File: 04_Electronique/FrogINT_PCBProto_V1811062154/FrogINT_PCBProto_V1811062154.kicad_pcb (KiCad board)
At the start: 2 copper layers, 31 parts, among them J1 USB_B_Mini, J2 Conn_01x01_Female, J3 AVR-JTAG-10, Q1 PMV48XP, Q2 PMV48XP, SW1 SW_SPST, SW2 SW_SPST, U1 NCP1117-5.0_SOT223, U2 LP2985-3.3, U3 ATmega16U4RC-AU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

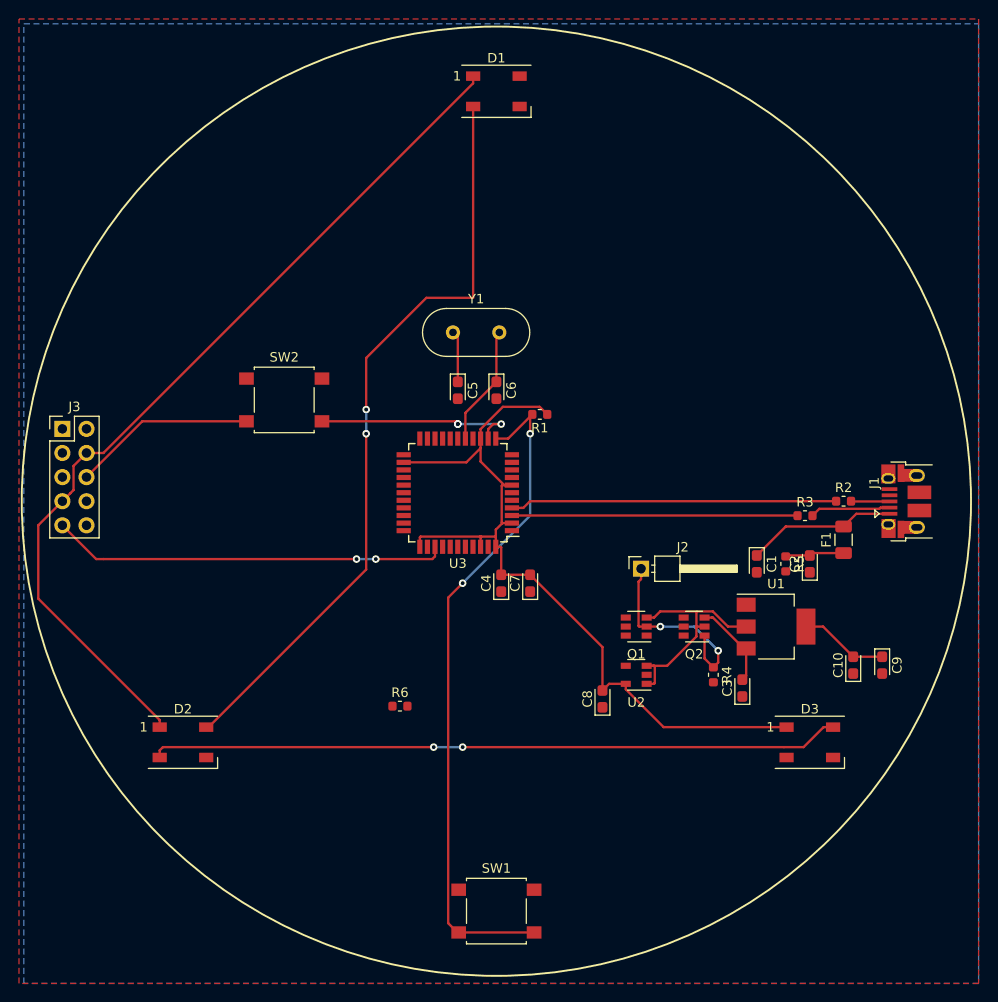
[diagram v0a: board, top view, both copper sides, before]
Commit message: Finalisation du routage + création d'un nouveau routage "Push" pour tester une nouvelle implémentation + Ajout d'un Logo en silkscreen & Copper.
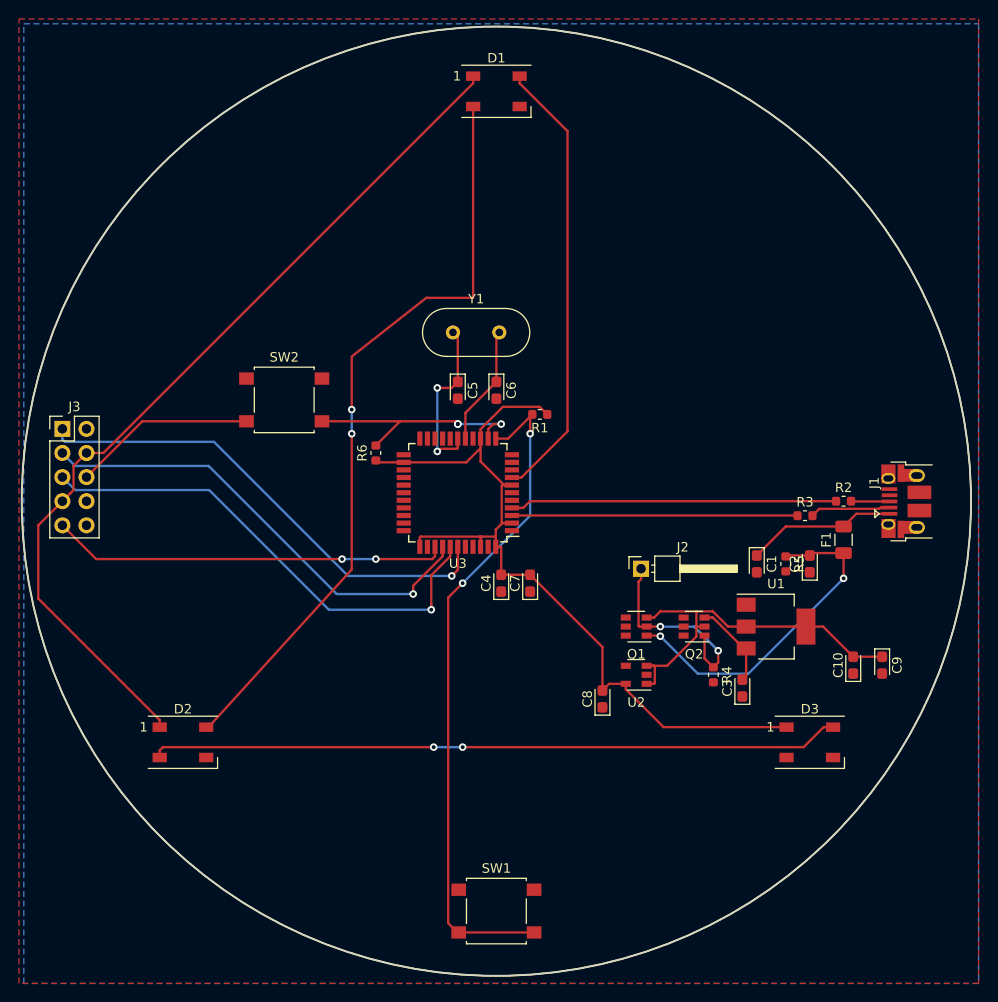
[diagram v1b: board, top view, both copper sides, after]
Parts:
- moved R6 26.8 mm to (133.9, 93.2), turned to 90 degrees
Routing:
- net Net-(J3-Pad5): track 0.00 -> 52.1 mm, vias 0 -> 1
- net Net-(J3-Pad1): track 0.00 -> 51.4 mm, vias 0 -> 1
- net Net-(J3-Pad3): track 0.00 -> 49.4 mm, vias 0 -> 1
- net Net-(D1-Pad4): track 0.00 -> 47.4 mm
- net VBUS: track 6.24 -> 35.5 mm, vias 0 -> 2
- net Net-(C5-Pad1): track 5.42 -> 17.8 mm, vias 0 -> 2
- net +5V: track 34.3 -> 40.6 mm
- net /reset: track 40.9 -> 44.5 mm
- net +3V3: track 181.5 -> 184.5 mm
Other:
- board outline added: 100 x 100 mm

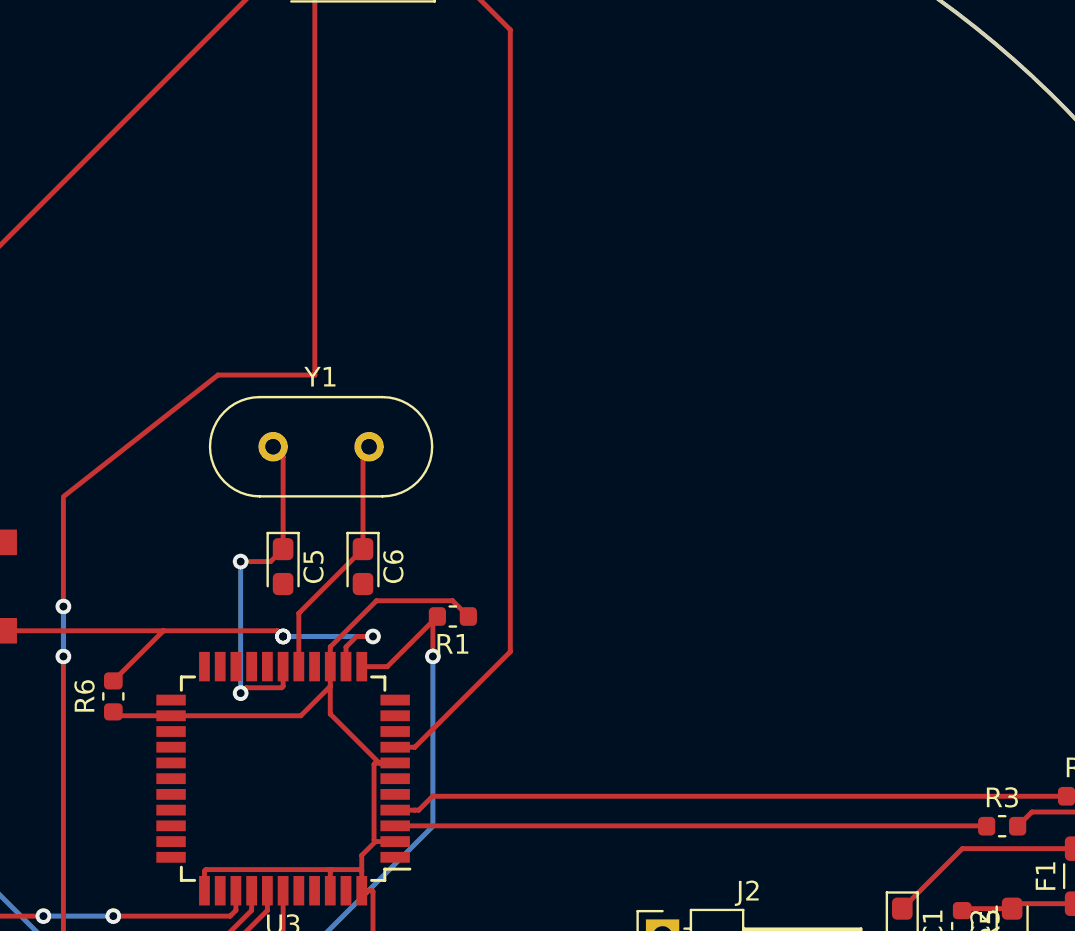
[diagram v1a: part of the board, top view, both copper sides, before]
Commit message: Creation d'un touch Pad et Ajout du composant TTP223.
Création des librairies équivalentes pour le pad dans Samsac.
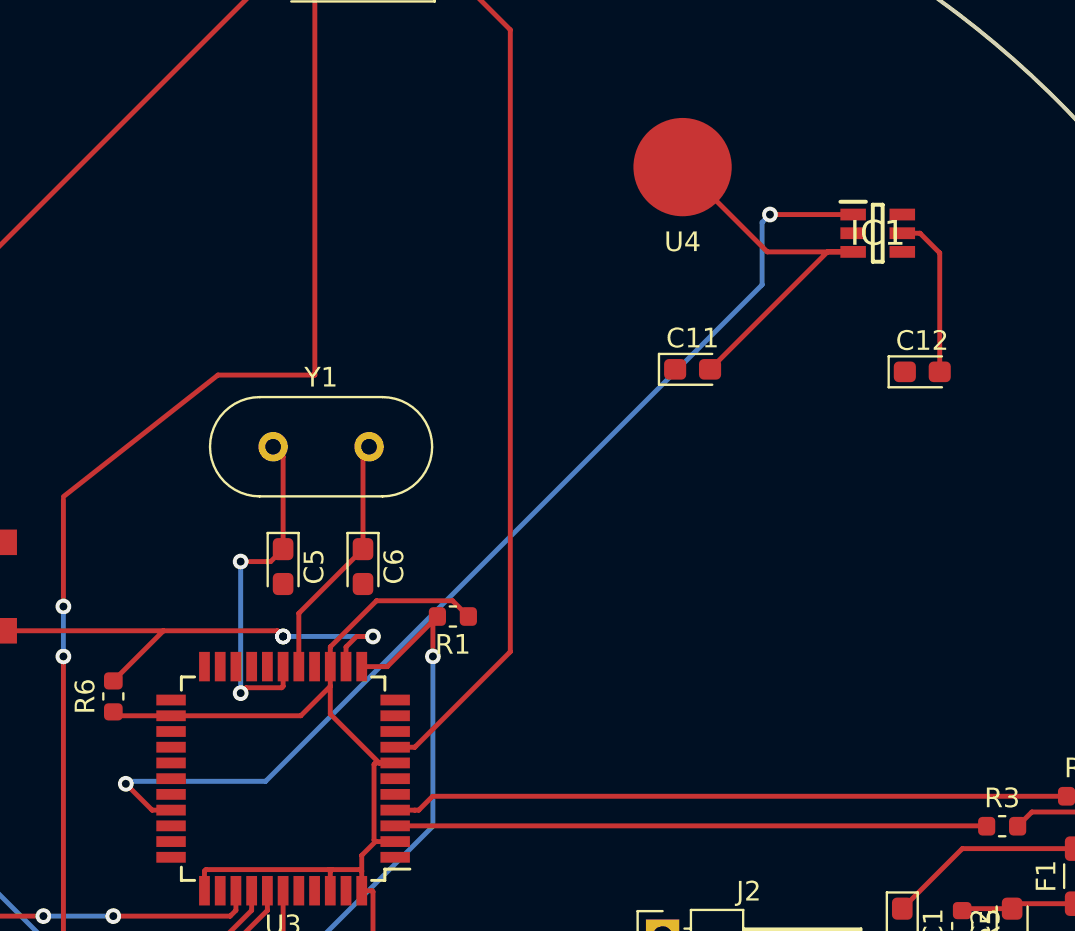
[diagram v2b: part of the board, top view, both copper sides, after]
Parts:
- added C11: 22pF, FTA_FrogINT_Library_Footprint_Package:CP_EIA-2012-12_Kemet-R, F.Cu at (163.3, 76.6)
- added C12: 100nF, FTA_FrogINT_Library_Footprint_Package:CP_EIA-2012-12_Kemet-R, F.Cu at (175.0, 76.7)
- added IC1: TTP223-BA6, SamacSys_Parts:SOT95P285X126-6N, F.Cu at (172.7, 69.7)
- added U4: TouchSensePanel, SamacSys_PCB_Library:TouchSensePad, F.Cu at (162.8, 66.3)
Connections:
- U3 pad 30: Net-(U3-Pad30) -> /Input_Int_Touch
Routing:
- net /Input_Int_Touch: track 0.00 -> 53.7 mm, vias 0 -> 2
- net /Cap-TouchSensor: track 0.00 -> 20.2 mm
- net +5V: track 40.6 -> 49.0 mm

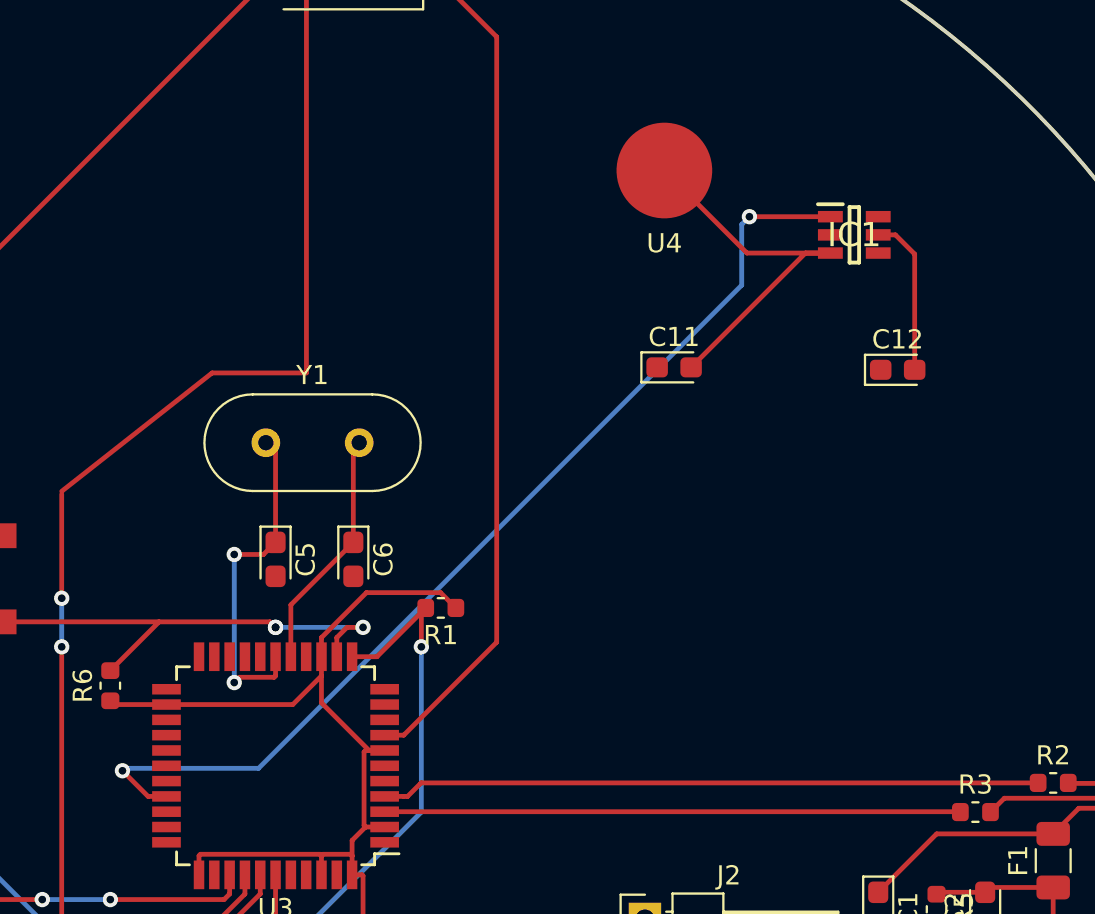
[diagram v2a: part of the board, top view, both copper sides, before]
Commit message: ***Commit du 14/01/2019 suite aux modifications du 11/01/2019
            • Création d'un nouveau composant (schéma + PCB) TouchSense sur la librairie FTA (et non plus Samacsys)
	• Ajout de ce composant dans le design courant
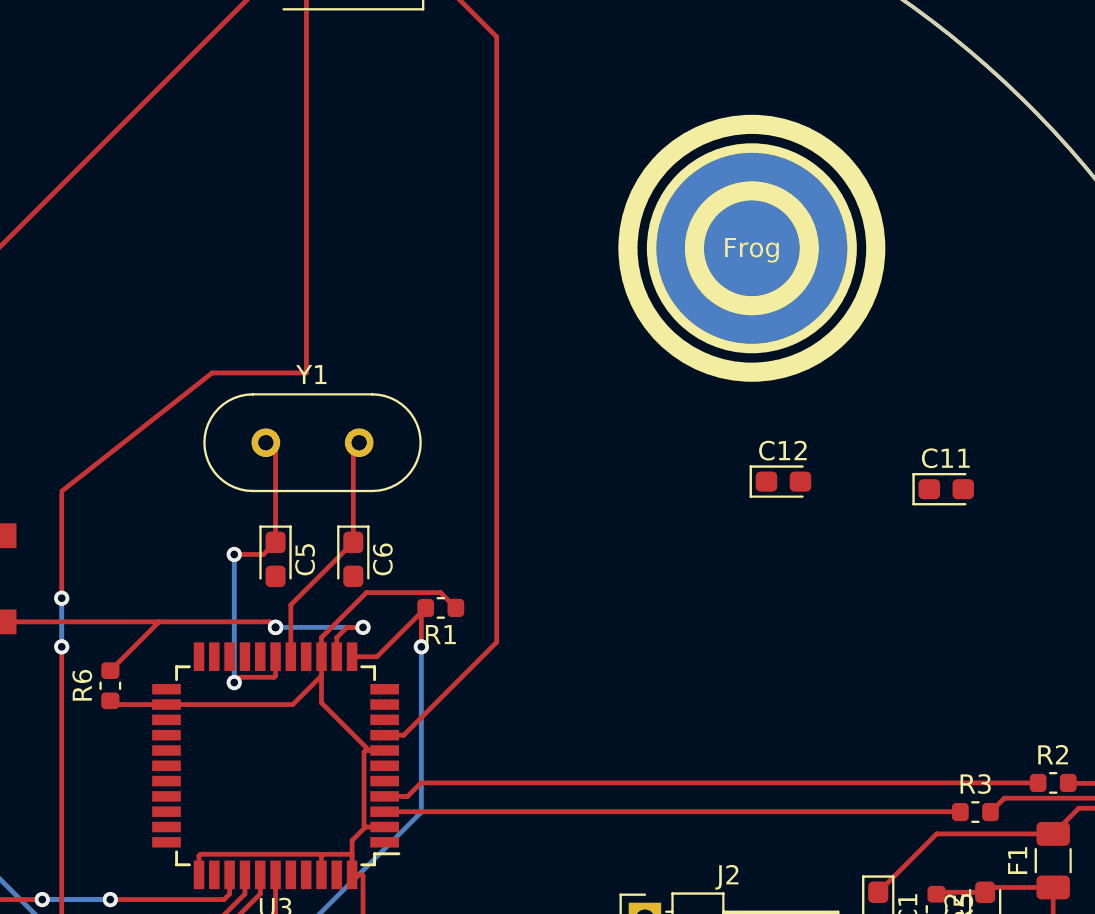
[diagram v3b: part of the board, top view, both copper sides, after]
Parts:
- removed IC1: TTP223-BA6, SamacSys_Parts:SOT95P285X126-6N
- removed U4: TouchSensePanel, SamacSys_PCB_Library:TouchSensePad
- added TS1: TouchSense, FTA_FrogINT_Library_Footprint_Package:CapacitiveTouchSense_Bottom_10mm, F.Cu at (167.4, 70.4)
- moved C11 15.6 mm to (177.5, 82.9)
- moved C12 8.35 mm to (169.0, 82.5)
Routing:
- net /Input_Int_Touch: track 53.7 -> 0.00 mm, vias 2 -> 0
- net /Cap-TouchSensor: track 20.2 -> 0.00 mm
- net +5V: track 49.0 -> 40.6 mm
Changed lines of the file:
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@@
     (thickness 1.6)
     (drawings 2)
-    (tracks 242)
+    (tracks 225)
     (zones 0)
-    (modules 35)
+    (modules 34)
     (nets 48)
   )
@@
     )
   )
+  (module FTA_FrogINT_Library_Footprint_Package:CapacitiveTouchSense_Bottom_10mm (layer F.Cu)
+    (at 167.386 70.358)
+    (tags "Capacitive Touch Sense button switch")
+    (attr smd)
+    (fp_text reference TS1 (at 0 8.89) (layer B.SilkS)
+      (effects (font (size 1 1) (thickness 0.15)) (justify mirror))
+    )
+    (fp_text value TouchSense (at 0 -8.89) (layer F.Fab)
+      (effects (font (size 1 1) (thickness 0.15)))
+    )
+    (fp_circle (center 0 0) (end 6.475755 0) (layer F.SilkS) (width 1))
+    (fp_circle (center 0 0) (end 5.236344 0) (layer F.SilkS) (width 0.5))
+    (fp_circle (center 0 0) (end 3 0) (layer F.SilkS) (width 1))
+    (fp_text user Frog (at 0 0) (layer F.SilkS)
+      (effects (font (size 1 1) (thickness 0.15)))
+    )
+    (fp_circle (center 0 0) (end 7.62 0) (layer B.SilkS) (width 0.15))
+    (fp_line (start -12.7 -8.89) (end 12.7 -8.89) (layer B.CrtYd) (width 0.15))
+    (fp_line (start 12.7 -8.89) (end 12.7 8.89) (layer B.CrtYd) (width 0.15))
+    (fp_line (start 12.7 8.89) (end -12.7 8.89) (layer B.CrtYd) (width 0.15))
+    (fp_line (start -12.7 8.89) (end -12.7 -8.89) (layer B.CrtYd) (width 0.15))
+    (fp_line (start -12.7 -8.89) (end 12.7 -8.89) (layer F.CrtYd) (width 0.15))
+    (fp_line (start 12.7 -8.89) (end 12.7 8.89) (layer F.CrtYd) (width 0.15))
+    (fp_line (start 12.7 8.89) (end -12.7 8.89) (layer F.CrtYd) (width 0.15))
+    (pad 1 smd circle (at 0 0) (size 10 10) (layers B.Cu B.Paste B.Mask)
+      (net 46 /Cap-TouchSensor))
+  )
   (module FTA_FrogINT_Library_Footprint_Package:CP_EIA-2012-12_Kemet-R (layer F.Cu)
-    (at 163.3235 76.581)
+    (at 177.546 82.947001)
     (descr "Tantalum Capacitor SMD Kemet-R (2012-12 Metric), IPC_7351 nominal, (Body size from: https://www.vishay.com/docs/40182/tmch.pdf), generated with kicad-footprint-generator")
     (tags "capacitor tantalum")
@@
   )
   (module FTA_FrogINT_Library_Footprint_Package:CP_EIA-2012-12_Kemet-R (layer F.Cu)
-    (at 175.0075 76.708)
+    (at 169.0385 82.55)
     (descr "Tantalum Capacitor SMD Kemet-R (2012-12 Metric), IPC_7351 nominal, (Body size from: https://www.vishay.com/docs/40182/tmch.pdf), generated with kicad-footprint-generator")
     (tags "capacitor tantalum")
@@
       (rotate (xyz -90 0 0))
     )
-  )
-  (module SamacSys_Parts:SOT95P285X126-6N (layer F.Cu)
-    (at 172.74 69.657)
-    (descr SOT-23-6L)
-    (tags "Integrated Circuit")
-    (attr smd)
-    (fp_text reference IC1 (at 0 0) (layer F.SilkS)
-      (effects (font (size 1.27 1.27) (thickness 0.254)))
-    )
-    (fp_text value TTP223-BA6 (at 0 0) (layer F.SilkS) hide
-      (effects (font (size 1.27 1.27) (thickness 0.254)))
-    )
-    (fp_line (start -2.15 -1.8) (end 2.15 -1.8) (layer Dwgs.User) (width 0.05))
-    (fp_line (start 2.15 -1.8) (end 2.15 1.8) (layer Dwgs.User) (width 0.05))
-    (fp_line (start 2.15 1.8) (end -2.15 1.8) (layer Dwgs.User) (width 0.05))
-    (fp_line (start -2.15 1.8) (end -2.15 -1.8) (layer Dwgs.User) (width 0.05))
-    (fp_line (start -0.825 -1.45) (end 0.825 -1.45) (layer Dwgs.User) (width 0.1))
-    (fp_line (start 0.825 -1.45) (end 0.825 1.45) (layer Dwgs.User) (width 0.1))
-    (fp_line (start 0.825 1.45) (end -0.825 1.45) (layer Dwgs.User) (width 0.1))
-    (fp_line (start -0.825 1.45) (end -0.825 -1.45) (layer Dwgs.User) (width 0.1))
-    (fp_line (start -0.825 -0.5) (end 0.125 -1.45) (layer Dwgs.User) (width 0.1))
-    (fp_line (start -0.25 -1.45) (end 0.25 -1.45) (layer F.SilkS) (width 0.2))
-    (fp_line (start 0.25 -1.45) (end 0.25 1.45) (layer F.SilkS) (width 0.2))
-    (fp_line (start 0.25 1.45) (end -0.25 1.45) (layer F.SilkS) (width 0.2))
-    (fp_line (start -0.25 1.45) (end -0.25 -1.45) (layer F.SilkS) (width 0.2))
-    (fp_line (start -1.9 -1.6) (end -0.6 -1.6) (layer F.SilkS) (width 0.2))
-    (pad 1 smd rect (at -1.25 -0.95 90) (size 0.6 1.3) (layers F.Cu F.Paste F.Mask)
-      (net 47 /Input_Int_Touch))
-    (pad 2 smd rect (at -1.25 0 90) (size 0.6 1.3) (layers F.Cu F.Paste F.Mask)
-      (net 1 GND))
-    (pad 3 smd rect (at -1.25 0.95 90) (size 0.6 1.3) (layers F.Cu F.Paste F.Mask)
-      (net 46 /Cap-TouchSensor))
-    (pad 4 smd rect (at 1.25 0.95 90) (size 0.6 1.3) (layers F.Cu F.Paste F.Mask)
-      (net 1 GND))
-    (pad 5 smd rect (at 1.25 0 90) (size 0.6 1.3) (layers F.Cu F.Paste F.Mask)
-      (net 8 +5V))
-    (pad 6 smd rect (at 1.25 -0.95 90) (size 0.6 1.3) (layers F.Cu F.Paste F.Mask)
-      (net 1 GND))
-  )
-  (module SamacSys_PCB_Library:TouchSensePad (layer F.Cu)
-    (at 162.814 66.294)
-    (tags "Touch Sense Pad")
-    (attr smd)
-    (fp_text reference U4 (at 0 3.81) (layer F.SilkS)
-      (effects (font (size 1 1) (thickness 0.15)))
-    )
-    (fp_text value TouchSensePanel (at 0 -3.81) (layer F.Fab)
-      (effects (font (size 1 1) (thickness 0.15)))
-    )
-    (pad 1 smd circle (at 0 0) (size 5 5) (layers F.Cu F.Paste F.Mask)
-      (net 46 /Cap-TouchSensor))
   )
   (gr_circle (center 146.558 98.298) (end 196.558 98.298) (layer Edge.Cuts) (width 0.15))
@@
   (segment (start 177.922 111.506) (end 172.872 111.506) (width 0.25) (layer F.Cu) (net 8))
   (segment (start 179.172 111.506) (end 177.922 111.506) (width 0.25) (layer F.Cu) (net 8))
-  (segment (start 174.89 69.657) (end 173.99 69.657) (width 0.25) (layer F.Cu) (net 8))
-  (segment (start 175.895 70.662) (end 174.89 69.657) (width 0.25) (layer F.Cu) (net 8))
-  (segment (start 175.895 76.708) (end 175.895 70.662) (width 0.25) (layer F.Cu) (net 8))
   (segment (start 149.194 95.803001) (end 154.051 90.946001) (width 0.25) (layer F.Cu) (net 9))
   (segment (start 148.194 95.803001) (end 149.194 95.803001) (width 0.25) (layer F.Cu) (net 9))
@@
   (segment (start 178.263501 99.803001) (end 178.2825 99.822) (width 0.25) (layer F.Cu) (net 24))
   (segment (start 148.194 99.803001) (end 178.263501 99.803001) (width 0.25) (layer F.Cu) (net 24))
-  (segment (start 167.127 70.607) (end 162.814 66.294) (width 0.25) (layer F.Cu) (net 46))
-  (segment (start 171.49 70.607) (end 167.127 70.607) (width 0.25) (layer F.Cu) (net 46))
-  (segment (start 170.185 70.607) (end 164.211 76.581) (width 0.25) (layer F.Cu) (net 46))
-  (segment (start 171.49 70.607) (end 170.185 70.607) (width 0.25) (layer F.Cu) (net 46))
-  (via (at 167.259 68.707) (size 0.8) (drill 0.4) (layers F.Cu B.Cu) (net 47))
-  (segment (start 171.49 68.707) (end 167.259 68.707) (width 0.25) (layer F.Cu) (net 47))
-  (segment (start 166.859001 69.106999) (end 166.859001 72.281999) (width 0.25) (layer B.Cu) (net 47))
-  (segment (start 167.259 68.707) (end 166.859001 69.106999) (width 0.25) (layer B.Cu) (net 47))
-  (segment (start 166.859001 72.281999) (end 141.605 97.536) (width 0.25) (layer B.Cu) (net 47))
-  (via (at 134.493 97.663) (size 0.8) (drill 0.4) (layers F.Cu B.Cu) (net 47))
-  (segment (start 141.605 97.536) (end 134.62 97.536) (width 0.25) (layer B.Cu) (net 47))
-  (segment (start 134.62 97.536) (end 134.493 97.663) (width 0.25) (layer B.Cu) (net 47))
-  (segment (start 135.833001 99.003001) (end 136.794 99.003001) (width 0.25) (layer F.Cu) (net 47))
-  (segment (start 134.493 97.663) (end 135.833001 99.003001) (width 0.25) (layer F.Cu) (net 47))
   (zone (net 1) (net_name GND) (layer F.Cu) (hatch edge 0.508)
     (connect_pads (clearance 0.508))
     (min_thickness 0.254)
-    (fill yes (arc_segments 16) (thermal_gap 0.508) (thermal_bridge_width 0.508))
+    (fill (arc_segments 16) (thermal_gap 0.508) (thermal_bridge_width 0.508))
     (polygon
       (pts
@@
     (connect_pads (clearance 0.508))
     (min_thickness 0.254)
-    (fill yes (arc_segments 16) (thermal_gap 0.508) (thermal_bridge_width 0.508))
+    (fill (arc_segments 16) (thermal_gap 0.508) (thermal_bridge_width 0.508))
     (polygon
       (pts
